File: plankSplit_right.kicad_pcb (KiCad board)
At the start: 2 copper layers, 121.3 x 127.1 mm, 90 parts, among them K1 XLR3, P1 USB_A, SW0:1 SPACE, SW0:2 ENTER, SW0:3 ALTGR, SW0:4 FN_R, SW0:5 MOD4, SW0:6 CTRL_R, SW1:1 B, SW1:2 M, SW1:3 ,, SW1:4 ., SW1:5 J, SW1:6 END, SW2:1 S, SW2:2 N, SW2:3 R, SW2:4 T, SW2:5 D, SW2:6 Y, SW3:1 K, SW3:2 H, SW3:3 G, SW3:4 F, SW3:5 Q, SW3:6 ẞ, SW4:1 6, SW4:2 7, SW4:3 8, SW4:4 9, SW4:5 0, SW4:6 BCKSPC, U1 ATmega32U4-AU, X1 CRYSTAL

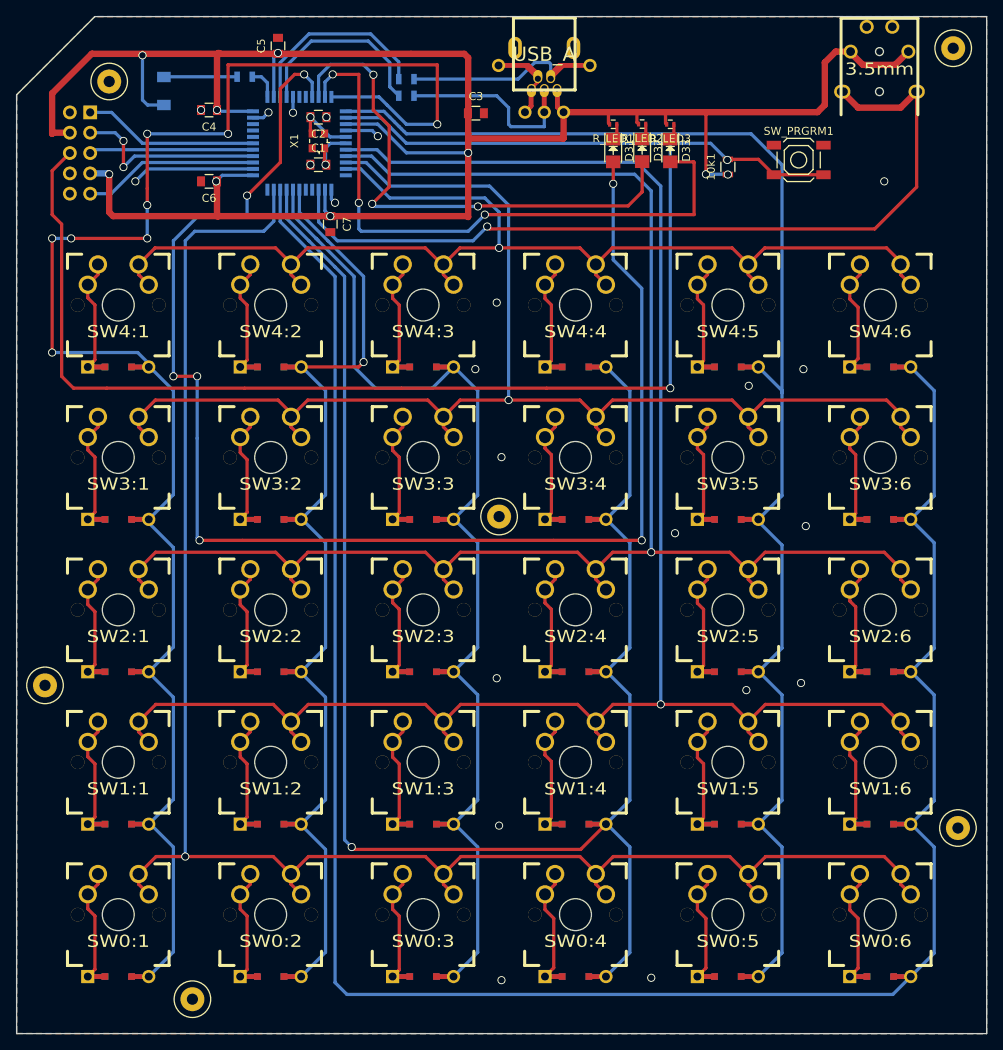
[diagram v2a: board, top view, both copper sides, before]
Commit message: Added more vias
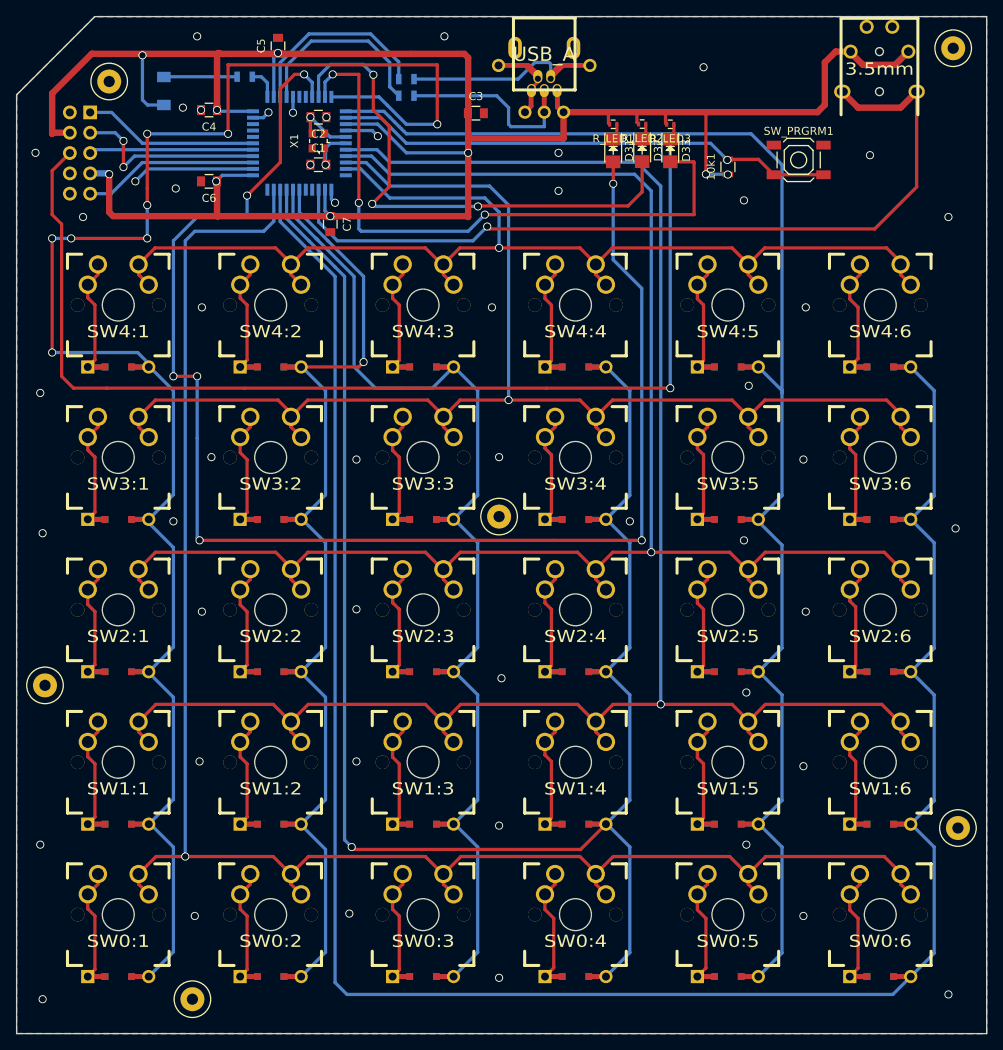
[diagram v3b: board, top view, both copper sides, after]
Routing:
- net /UGND: vias 8 -> 51
- net (no net): vias 14 -> 0
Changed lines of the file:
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@@
   (general
     (links 219)
-    (no_connects 2)
+    (no_connects 1)
     (area 19.065768 12.137295 140.47537 139.664856)
     (thickness 1.6)
     (drawings 6)
-    (tracks 840)
+    (tracks 869)
     (zones 0)
     (modules 90)
@@
     (pad 0 thru_hole circle (at -5.08 0) (size 1.7018 1.7018) (drill 1.701799) (layers *.Cu)
       (solder_mask_margin -0.254) (zone_connect 2))
-    (pad 0 thru_hole circle (at 5.08 0) (size 1.7018 1.7018) (drill 1.701799) (layers *.Cu)
+    (pad 1 thru_hole circle (at 5.08 0) (size 1.7018 1.7018) (drill 1.701799) (layers *.Cu)
       (solder_mask_margin -0.254) (zone_connect 2))
     (pad 1 thru_hole circle (at 3.81 -2.54) (size 2.286 2.286) (drill 1.498599) (layers *.Cu *.SilkS *.Mask)
@@
   (gr_line (start 140.400369 139.589855) (end 19.140769 139.589855) (angle 90) (layer Edge.Cuts) (width 0.15))
   (gr_line (start 140.400369 129.810855) (end 140.400369 139.589855) (angle 90) (layer Edge.Cuts) (width 0.15))
-  (via (at 79.750249 67.530055) (size 1.016) (drill 0.7874) (layers F.Cu B.Cu) (net 0))
-  (via (at 79.453069 113.592955) (size 1.016) (drill 0.7874) (layers F.Cu B.Cu) (net 0))
-  (via (at 98.472589 132.612475) (size 1.016) (drill 0.7874) (layers F.Cu B.Cu) (net 0))
-  (via (at 101.444389 77.039815) (size 1.016) (drill 0.7874) (layers F.Cu B.Cu) (net 0))
-  (via (at 76.481269 56.534395) (size 1.016) (drill 0.7874) (layers F.Cu B.Cu) (net 0))
-  (via (at 127.596229 33.057175) (size 1.016) (drill 0.7874) (layers F.Cu B.Cu) (net 0))
-  (via (at 79.750249 132.909655) (size 1.016) (drill 0.7874) (layers F.Cu B.Cu) (net 0))
-  (via (at 110.656969 58.614655) (size 1.016) (drill 0.7874) (layers F.Cu B.Cu) (net 0))
-  (via (at 110.359789 96.653695) (size 1.016) (drill 0.7874) (layers F.Cu B.Cu) (net 0))
-  (via (at 117.194929 95.762155) (size 1.016) (drill 0.7874) (layers F.Cu B.Cu) (net 0))
-  (via (at 117.789289 76.148275) (size 1.016) (drill 0.7874) (layers F.Cu B.Cu) (net 0))
-  (via (at 117.492109 56.534395) (size 1.016) (drill 0.7874) (layers F.Cu B.Cu) (net 0))
-  (via (at 79.155889 48.213355) (size 1.016) (drill 0.7874) (layers F.Cu B.Cu) (net 0))
-  (via (at 79.155889 95.167795) (size 1.016) (drill 0.7874) (layers F.Cu B.Cu) (net 0))
   (segment (start 59.244829 40.486675) (end 76.184089 40.486675) (width 0.4064) (layer B.Cu) (net 1))
   (segment (start 56.889949 38.131795) (end 59.244829 40.486675) (width 0.4064) (layer B.Cu) (net 1))
@@
   (segment (start 55.975849 15.523555) (end 63.108169 15.523555) (width 0.4064) (layer B.Cu) (net 46))
   (segment (start 52.889949 18.609455) (end 55.975849 15.523555) (width 0.4064) (layer B.Cu) (net 46))
+  (via (at 135.620089 37.514875) (size 1.016) (drill 0.7874) (layers F.Cu B.Cu) (net 47))
+  (via (at 136.511629 76.445455) (size 1.016) (drill 0.7874) (layers F.Cu B.Cu) (net 47))
+  (via (at 135.620089 134.692735) (size 1.016) (drill 0.7874) (layers F.Cu B.Cu) (net 47))
+  (via (at 117.492109 124.885795) (size 1.016) (drill 0.7874) (layers F.Cu B.Cu) (net 47))
+  (via (at 117.492109 106.163455) (size 1.016) (drill 0.7874) (layers F.Cu B.Cu) (net 47))
+  (via (at 117.789289 86.846755) (size 1.016) (drill 0.7874) (layers F.Cu B.Cu) (net 47))
+  (via (at 117.492109 67.827235) (size 1.016) (drill 0.7874) (layers F.Cu B.Cu) (net 47))
+  (via (at 117.789289 48.807715) (size 1.016) (drill 0.7874) (layers F.Cu B.Cu) (net 47))
+  (via (at 38.739409 75.553915) (size 1.016) (drill 0.7874) (layers F.Cu B.Cu) (net 47))
+  (via (at 27.446569 37.514875) (size 1.016) (drill 0.7874) (layers F.Cu B.Cu) (net 47))
+  (via (at 42.305569 48.807715) (size 1.016) (drill 0.7874) (layers F.Cu B.Cu) (net 47))
+  (via (at 43.494289 67.530055) (size 1.016) (drill 0.7874) (layers F.Cu B.Cu) (net 47))
+  (via (at 42.305569 86.846755) (size 1.016) (drill 0.7874) (layers F.Cu B.Cu) (net 47))
+  (via (at 42.008389 105.569095) (size 1.016) (drill 0.7874) (layers F.Cu B.Cu) (net 47))
+  (via (at 41.414029 124.885795) (size 1.016) (drill 0.7874) (layers F.Cu B.Cu) (net 47))
+  (via (at 22.394509 135.287095) (size 1.016) (drill 0.7874) (layers F.Cu B.Cu) (net 47))
+  (via (at 22.097329 115.970395) (size 1.016) (drill 0.7874) (layers F.Cu B.Cu) (net 47))
+  (via (at 22.394509 77.039815) (size 1.016) (drill 0.7874) (layers F.Cu B.Cu) (net 47))
+  (via (at 41.711209 14.929195) (size 1.016) (drill 0.7874) (layers F.Cu B.Cu) (net 47))
+  (via (at 72.617929 14.929195) (size 1.016) (drill 0.7874) (layers F.Cu B.Cu) (net 47))
+  (via (at 105.010549 18.792535) (size 1.016) (drill 0.7874) (layers F.Cu B.Cu) (net 47))
+  (via (at 86.882569 29.491015) (size 1.016) (drill 0.7874) (layers F.Cu B.Cu) (net 47))
+  (via (at 86.882569 34.245895) (size 1.016) (drill 0.7874) (layers F.Cu B.Cu) (net 47))
+  (via (at 22.097329 59.506195) (size 1.016) (drill 0.7874) (layers F.Cu B.Cu) (net 47))
+  (via (at 21.502969 29.491015) (size 1.016) (drill 0.7874) (layers F.Cu B.Cu) (net 47))
+  (via (at 39.928129 23.844595) (size 1.016) (drill 0.7874) (layers F.Cu B.Cu) (net 47))
+  (via (at 39.036589 33.948715) (size 1.016) (drill 0.7874) (layers F.Cu B.Cu) (net 47))
+  (via (at 61.622269 67.827235) (size 1.016) (drill 0.7874) (layers F.Cu B.Cu) (net 47))
+  (via (at 61.622269 86.549575) (size 1.016) (drill 0.7874) (layers F.Cu B.Cu) (net 47))
+  (via (at 61.622269 105.569095) (size 1.016) (drill 0.7874) (layers F.Cu B.Cu) (net 47))
+  (via (at 60.730729 124.588615) (size 1.016) (drill 0.7874) (layers F.Cu B.Cu) (net 47))
+  (via (at 95.797969 75.553915) (size 1.016) (drill 0.7874) (layers F.Cu B.Cu) (net 47))
+  (via (at 78.561529 48.807715) (size 1.016) (drill 0.7874) (layers F.Cu B.Cu) (net 47))
+  (via (at 79.453069 67.530055) (size 1.016) (drill 0.7874) (layers F.Cu B.Cu) (net 47))
+  (via (at 79.750249 95.167795) (size 1.016) (drill 0.7874) (layers F.Cu B.Cu) (net 47))
+  (via (at 79.453069 113.592955) (size 1.016) (drill 0.7874) (layers F.Cu B.Cu) (net 47))
+  (via (at 79.453069 132.612475) (size 1.016) (drill 0.7874) (layers F.Cu B.Cu) (net 47))
+  (via (at 110.359789 115.970395) (size 1.016) (drill 0.7874) (layers F.Cu B.Cu) (net 47))
+  (via (at 110.359789 96.950875) (size 1.016) (drill 0.7874) (layers F.Cu B.Cu) (net 47))
+  (via (at 110.062609 77.931355) (size 1.016) (drill 0.7874) (layers F.Cu B.Cu) (net 47))
+  (via (at 110.656969 58.614655) (size 1.016) (drill 0.7874) (layers F.Cu B.Cu) (net 47))
+  (via (at 110.062609 35.434615) (size 1.016) (drill 0.7874) (layers F.Cu B.Cu) (net 47))
+  (via (at 125.813149 29.788195) (size 1.016) (drill 0.7874) (layers F.Cu B.Cu) (net 47))
   (segment (start 53.689949 22.502295) (end 53.689949 24.474415) (width 0.4064) (layer B.Cu) (net 47))
   (via (at 53.689849 24.474515) (size 1.016) (drill 0.7874) (layers F.Cu B.Cu) (net 47))
